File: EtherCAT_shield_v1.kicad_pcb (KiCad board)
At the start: 2 copper layers, 71.1 x 81.3 mm, 105 parts, among them J1 RJ45-PULSETRANS, J2 RJ45-PULSETRANS, J3 GS3, J4 GS3, J5 GS3, J6 GS3, J7 GS2, J8 GS2, P1 CONN_02X10, P2 CONN_02X19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

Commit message: CHS GNDとPCB GNDを抵抗で接続
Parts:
- added R40: R, Resistors_SMD:R_1210, B.Cu at (151.9, 66.8)
- added R41: R, Resistors_SMD:R_1210, B.Cu at (114.8, 66.8)
- moved J8 3.76 mm to (147.5, 96.7)
- moved J7 3.70 mm to (147.4, 94.3)
- moved C25 3.00 mm to (148.2, 78.8)
- moved R19 3.00 mm to (150.5, 78.2)
- moved R20 3.00 mm to (152.2, 78.2)
- moved U2 3.00 mm to (146.9, 88.9)
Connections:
- R23 pad 1: Net-(J2-Pad11) -> +3V3
- R23 pad 2: +3V3 -> Net-(J2-Pad11)
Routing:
- net GND: track 470.4 -> 577.0 mm, vias 40 -> 57
- net Net-(J2-Pad11): track 1.75 -> 15.6 mm
- net GNDPWR: track 51.9 -> 59.9 mm
- net +3V3: track 248.2 -> 241.2 mm
- net /LAN9252/RUNLED: track 78.7 -> 83.0 mm
- net PA7: track 22.4 -> 18.4 mm
- net SIO3: track 13.9 -> 17.7 mm
- net SIO2: track 32.1 -> 35.8 mm
- net PA6: track 18.4 -> 14.9 mm
- net /LAN9252/LINKACTLED0: track 41.2 -> 44.4 mm
- net /LAN9252/LINKACTLED1: track 62.9 -> 66.0 mm
- net Net-(R20-Pad2): track 24.7 -> 22.1 mm
- net Net-(R19-Pad2): track 21.4 -> 18.8 mm
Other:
- board text added: "+3V3V"

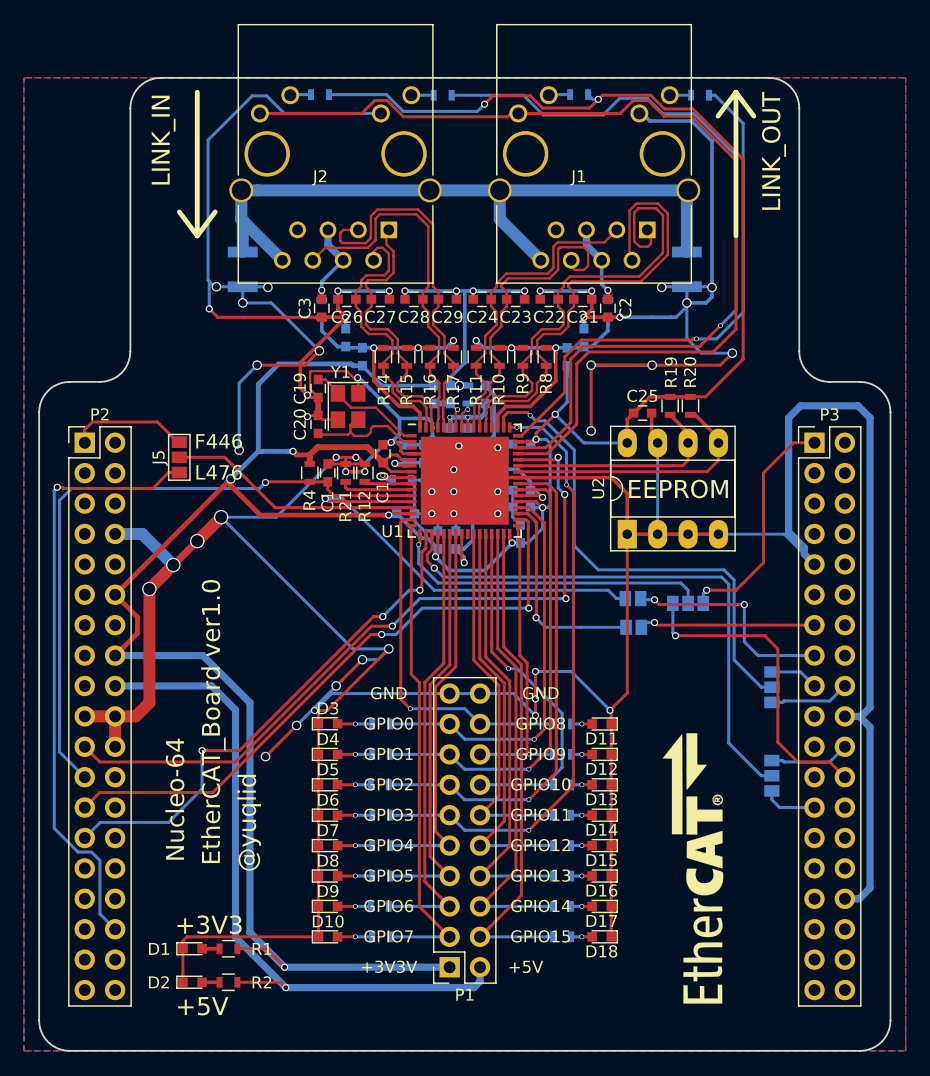
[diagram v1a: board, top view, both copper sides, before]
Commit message: GNDまわりの調整
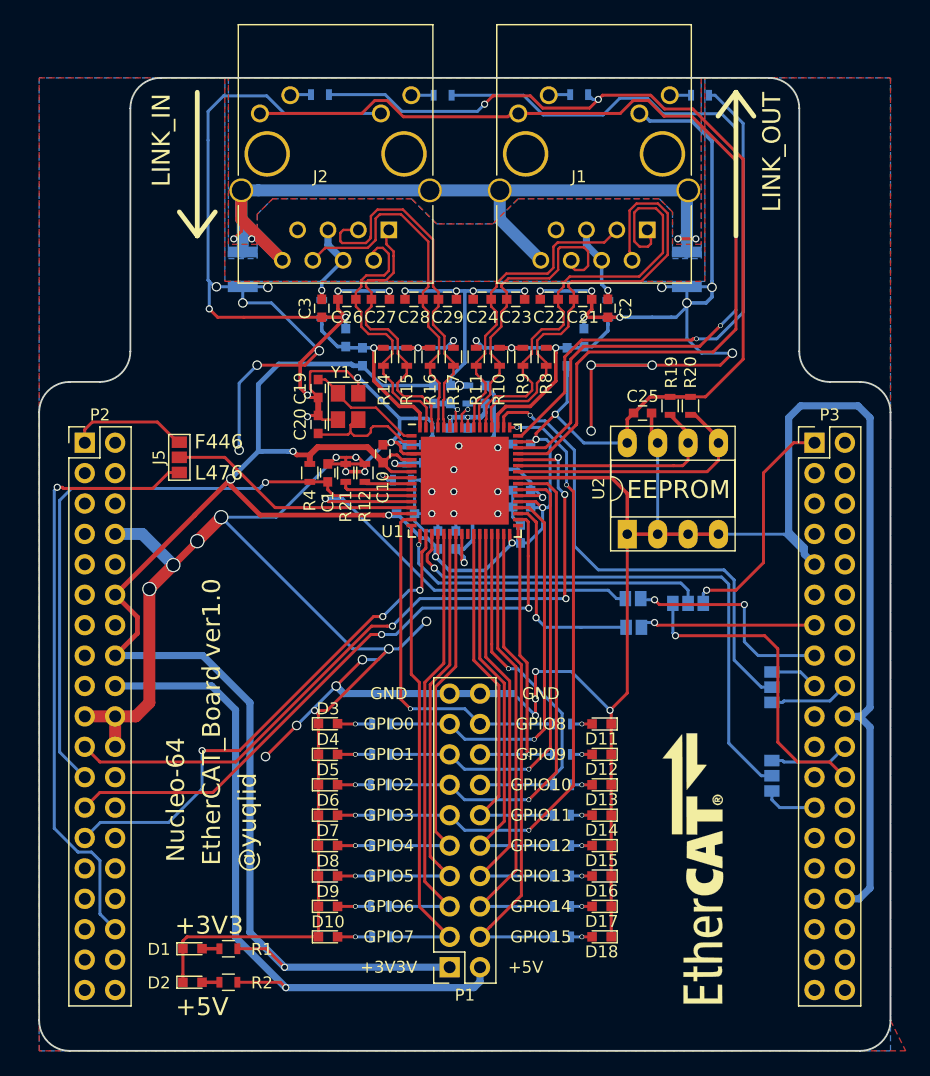
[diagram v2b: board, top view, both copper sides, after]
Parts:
- turned R23 to 180 degrees
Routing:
- net GNDPWR: track 59.9 -> 78.8 mm, vias 0 -> 4
- net Net-(J2-Pad11): track 15.6 -> 1.75 mm
- net +3V3: track 241.2 -> 255.0 mm
- net GND: track 577.0 -> 580.4 mm, vias 57 -> 58
- net /LAN9252/LINKACTLED1: track 66.0 -> 67.3 mm
- net RX2_P: track 31.4 -> 30.6 mm
- net RX2_N: track 31.2 -> 30.5 mm
- added copper zone on B.Cu, net GNDPWR
- added copper zone on F.Cu, net GNDPWR

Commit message: 抵抗とかコンデンサを追加
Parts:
- added C30: 10u, Capacitors_SMD:C_0805, F.Cu at (134.7, 128.8)
- added C31: 10u, Capacitors_SMD:C_0805, F.Cu at (132.1, 128.8)
- added C32: 10u, Capacitors_SMD:C_0805, F.Cu at (107.7, 88.5)
- added C33: 10u, Capacitors_SMD:C_0805, B.Cu at (119.8, 73.4)
- added R42: 10k, Resistors_SMD:R_0603, F.Cu at (156.8, 71.2)
- added R43: 10k, Resistors_SMD:R_0603, B.Cu at (157.6, 66.7)
- added R44: 10k, Resistors_SMD:R_0603, B.Cu at (155.0, 66.7)
- C9: moved to F.Cu
- moved C9 2.64 mm to (126.0, 88.3), turned to 270 degrees
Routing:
- net GND: track 580.4 -> 645.6 mm, vias 58 -> 70
- net +3V3: track 255.0 -> 259.0 mm
- net +5V: track 57.7 -> 60.4 mm
- net /LAN9252/LINKACTLED1: track 67.3 -> 68.9 mm
- net /LAN9252/LINKACTLED0: track 44.4 -> 45.8 mm

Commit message: viaの調整
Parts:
- added R45: 4.7k, Resistors_SMD:R_0603, B.Cu at (153.2, 86.6)
- moved C25 1.48 mm to (146.9, 78.1), turned to 90 degrees
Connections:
- U2 pad 1: GND -> Net-(R45-Pad1)
- U2 pad 2: GND -> Net-(R45-Pad1)
- U2 pad 3: GND -> Net-(R45-Pad1)
- U2 pad 7: GND -> Net-(R45-Pad1)
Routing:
- net Net-(R45-Pad1): track 0.00 -> 15.6 mm
- net GND: track 645.6 -> 631.7 mm, vias 70 -> 73
